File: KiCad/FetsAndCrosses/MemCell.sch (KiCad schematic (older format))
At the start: 0 parts

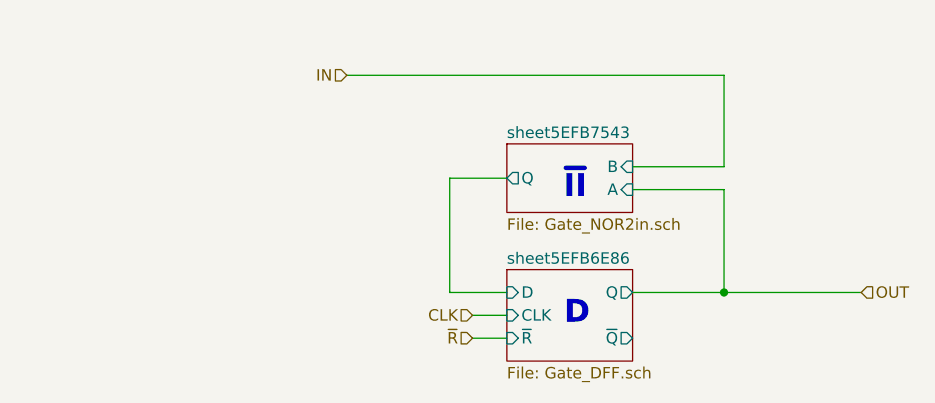
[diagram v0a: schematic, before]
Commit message: Schematic Done, Footprints assigned, ERC OK.
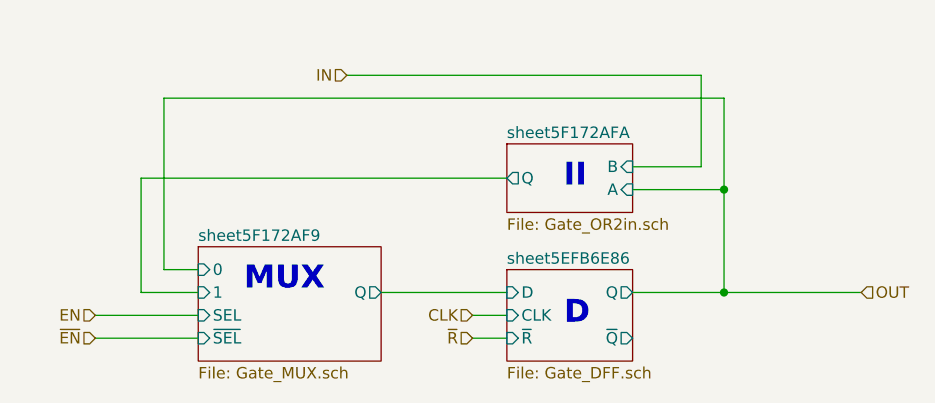
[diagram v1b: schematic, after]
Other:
- note added: "II"
- note added: "MUX"
- note removed: "~II"
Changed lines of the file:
@@
 $Descr A4 11693 8268
 encoding utf-8
-Sheet 216 400
+Sheet 17 389
 Title ""
 Date ""
@@
 F6 "~R" I L 5100 2600 50
 $EndSheet
+$Sheet
+S 3750 2200 800  500
+U 5F172B02
+F0 "sheet5F172AF9" 50
+F1 "Gate_MUX.sch" 50
+F2 "0" I L 3750 2300 50
+F3 "1" I L 3750 2400 50
+F4 "Q" O R 4550 2400 50
+F5 "SEL" I L 3750 2500 50
+F6 "~SEL" I L 3750 2600 50
+$EndSheet
+$Sheet
+S 5100 1750 550  300
+U 5F172B07
+F0 "sheet5F172AFA" 50
+F1 "Gate_OR2in.sch" 50
+F2 "A" I R 5650 1950 50
+F3 "B" I R 5650 1850 50
+F4 "Q" O L 5100 1900 50
+$EndSheet
 Text Notes 5350 2550 0    100  ~ 20
 D
-$Sheet
-S 5100 1750 550  300
-U 5EFB7548
-F0 "sheet5EFB7543" 50
-F1 "Gate_NOR2in.sch" 50
-F2 "Q" O L 5100 1900 50
-F3 "A" I R 5650 1950 50
-F4 "B" I R 5650 1850 50
-$EndSheet
-Text Notes 5450 2000 2    100  ~ 20
-~II
+Text HLabel 4400 1450 0    50   Input ~ 0
+IN
+Text HLabel 4950 2500 0    50   Input ~ 0
+CLK
+Text HLabel 4950 2600 0    50   Input ~ 0
+~R
+Text HLabel 6650 2400 2    50   Input ~ 0
+OUT
+Text Notes 3950 2400 0    100  ~ 20
+MUX
+Text Notes 5450 1950 2    100  ~ 20
+II
+Text HLabel 3300 2500 0    50   Input ~ 0
+EN
+Text HLabel 3300 2600 0    50   Input ~ 0
+~EN
 Wire Wire Line
 	5650 1950 6050 1950
@@
 	6050 2400 5650 2400
 Wire Wire Line
-	5650 1850 6050 1850
+	5650 1850 5950 1850
 Wire Wire Line
-	6050 1850 6050 1450
+	5950 1850 5950 1450
 Wire Wire Line
-	6050 1450 4400 1450
-Wire Wire Line
-	5100 1900 4850 1900
-Wire Wire Line
-	4850 1900 4850 2400
-Wire Wire Line
-	4850 2400 5100 2400
+	5950 1450 4400 1450
 Wire Wire Line
 	6050 2400 6650 2400
-Connection ~ 6050 2400
-Text HLabel 4400 1450 0    50   Input ~ 0
-IN
-Text HLabel 4950 2500 0    50   Input ~ 0
-CLK
 Wire Wire Line
 	4950 2500 5100 2500
-Text HLabel 4950 2600 0    50   Input ~ 0
-~R
 Wire Wire Line
 	4950 2600 5100 2600
-Text HLabel 6650 2400 2    50   Input ~ 0
-OUT
+Wire Wire Line
+	4550 2400 5100 2400
+Wire Wire Line
+	3750 2400 3500 2400
+Wire Wire Line
+	3500 2400 3500 1900
+Wire Wire Line
+	3500 1900 5100 1900
+Wire Wire Line
+	6050 1950 6050 1550
+Wire Wire Line
+	6050 1550 3600 1550
+Wire Wire Line
+	3600 1550 3600 2300
+Wire Wire Line
+	3600 2300 3750 2300
+Wire Wire Line
+	3750 2500 3300 2500
+Wire Wire Line
+	3750 2600 3300 2600
+Connection ~ 6050 2400
+Connection ~ 6050 1950
 $EndSCHEMATC

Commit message: First Draft Schematic Updates
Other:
- note added: "~&"
- note removed: "II"
- note removed: "MUX"
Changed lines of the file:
@@
 $Descr A4 11693 8268
 encoding utf-8
-Sheet 289 389
+Sheet 84 360
 Title ""
 Date "2020-07-05"
@@
 F6 "~R" I L 5100 2600 50
 $EndSheet
-$Sheet
-S 3750 2200 800  500
-U 5F172B02
-F0 "sheet5F172AF9" 50
-F1 "Gate_MUX.sch" 50
-F2 "0" I L 3750 2300 50
-F3 "1" I L 3750 2400 50
-F4 "Q" O R 4550 2400 50
-F5 "SEL" I L 3750 2500 50
-F6 "~SEL" I L 3750 2600 50
-$EndSheet
-$Sheet
-S 5100 1750 550  300
-U 5F172B07
-F0 "sheet5F172AFA" 50
-F1 "Gate_OR2in.sch" 50
-F2 "A" I R 5650 1950 50
-F3 "B" I R 5650 1850 50
-F4 "Q" O L 5100 1900 50
-$EndSheet
 Text Notes 5350 2550 0    100  ~ 20
 D
-Text HLabel 4400 1450 0    50   Input ~ 0
-IN
 Text HLabel 4950 2500 0    50   Input ~ 0
 CLK
@@
 Text HLabel 6650 2400 2    50   Input ~ 0
 OUT
-Text Notes 3950 2400 0    100  ~ 20
-MUX
-Text Notes 5450 1950 2    100  ~ 20
-II
-Text HLabel 3300 2500 0    50   Input ~ 0
-EN
-Text HLabel 3300 2600 0    50   Input ~ 0
-~EN
 Wire Wire Line
 	5650 1950 6050 1950
@@
 Wire Wire Line
 	6050 2400 5650 2400
-Wire Wire Line
-	5650 1850 5950 1850
-Wire Wire Line
-	5950 1850 5950 1450
-Wire Wire Line
-	5950 1450 4400 1450
 Wire Wire Line
 	6050 2400 6650 2400
@@
 Wire Wire Line
 	4550 2400 5100 2400
+Connection ~ 6050 2400
+$Sheet
+S 5100 1750 550  300
+U 5F46F15C
+F0 "sheet5F46F157" 50
+F1 "Gate_NAND2in.sch" 50
+F2 "Q" O L 5100 1900 50
+F3 "A" I R 5650 1950 50
+F4 "B" I R 5650 1850 50
+$EndSheet
+Text Notes 5450 2000 2    100  ~ 20
+~&
 Wire Wire Line
-	3750 2400 3500 2400
+	5650 1850 6050 1850
 Wire Wire Line
-	3500 2400 3500 1900
+	6050 1850 6050 1450
 Wire Wire Line
-	3500 1900 5100 1900
+	4400 1450 6050 1450
 Wire Wire Line
-	6050 1950 6050 1550
+	5100 1900 4550 1900
 Wire Wire Line
-	6050 1550 3600 1550
+	4550 1900 4550 2400
+$Sheet
+S 3850 1300 550  300
+U 5F46F779
+F0 "sheet5F46F774" 50
+F1 "Gate_NAND2in.sch" 50
+F2 "Q" O R 4400 1450 50
+F3 "A" I L 3850 1400 50
+F4 "B" I L 3850 1500 50
+$EndSheet
+Text Notes 4050 1550 0    100  ~ 20
+~&
+Text HLabel 3650 1500 0    50   Input ~ 0
+EN
+Text HLabel 3650 1400 0    50   Input ~ 0
+IN
 Wire Wire Line
-	3600 1550 3600 2300
+	3650 1400 3850 1400
 Wire Wire Line
-	3600 2300 3750 2300
-Wire Wire Line
-	3750 2500 3300 2500
-Wire Wire Line
-	3750 2600 3300 2600
-Connection ~ 6050 2400
-Connection ~ 6050 1950
+	3650 1500 3850 1500
 $EndSCHEMATC

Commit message: Updated Schematic
 - Fixed Mem cell
 - Fixed Draw LED to not light if last move wins game
 - Changed capacitor
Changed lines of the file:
@@
 $Descr A4 11693 8268
 encoding utf-8
-Sheet 54 360
-Title ""
-Date "2020-07-05"
-Rev "v0.0"
+Sheet 4 362
+Title "Fets and Crosses"
+Date "2020-09-15"
+Rev "v0.2"
 Comp "Philipp Schilk"
-Comment1 "c"
+Comment1 "Tic-Tac-Toe implementation from discrete-transistor CMOS logic"
 Comment2 ""
 Comment3 ""
-Comment4 ""
+Comment4 "https://github.com/TheSchilk/Fets_and_Crosses"
 $EndDescr
 $Sheet
@@
 	5650 1950 6050 1950
 Wire Wire Line
-	6050 1950 6050 2400
-Wire Wire Line
-	6050 2400 5650 2400
-Wire Wire Line
-	6050 2400 6650 2400
-Wire Wire Line
 	4950 2500 5100 2500
 Wire Wire Line
@@
 Wire Wire Line
 	4550 2400 5100 2400
-Connection ~ 6050 2400
 $Sheet
 S 5100 1750 550  300
@@
 Wire Wire Line
 	3650 1500 3850 1500
+Wire Wire Line
+	5650 2400 6650 2400
+Wire Wire Line
+	6050 1950 6050 2600
+Wire Wire Line
+	6050 2600 5650 2600
 $EndSCHEMATC
